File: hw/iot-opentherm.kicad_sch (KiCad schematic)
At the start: 32 parts, among them J1 USB_B_Micro, J2 Conn_01x02, J3 Conn_01x03, J4 Conn_02x06_Odd_Even, J5 Conn_01x02, Q1 BC858, U1 AMS1117-3.3, U2 ESP-12S, U3 PC817, U4 PC817

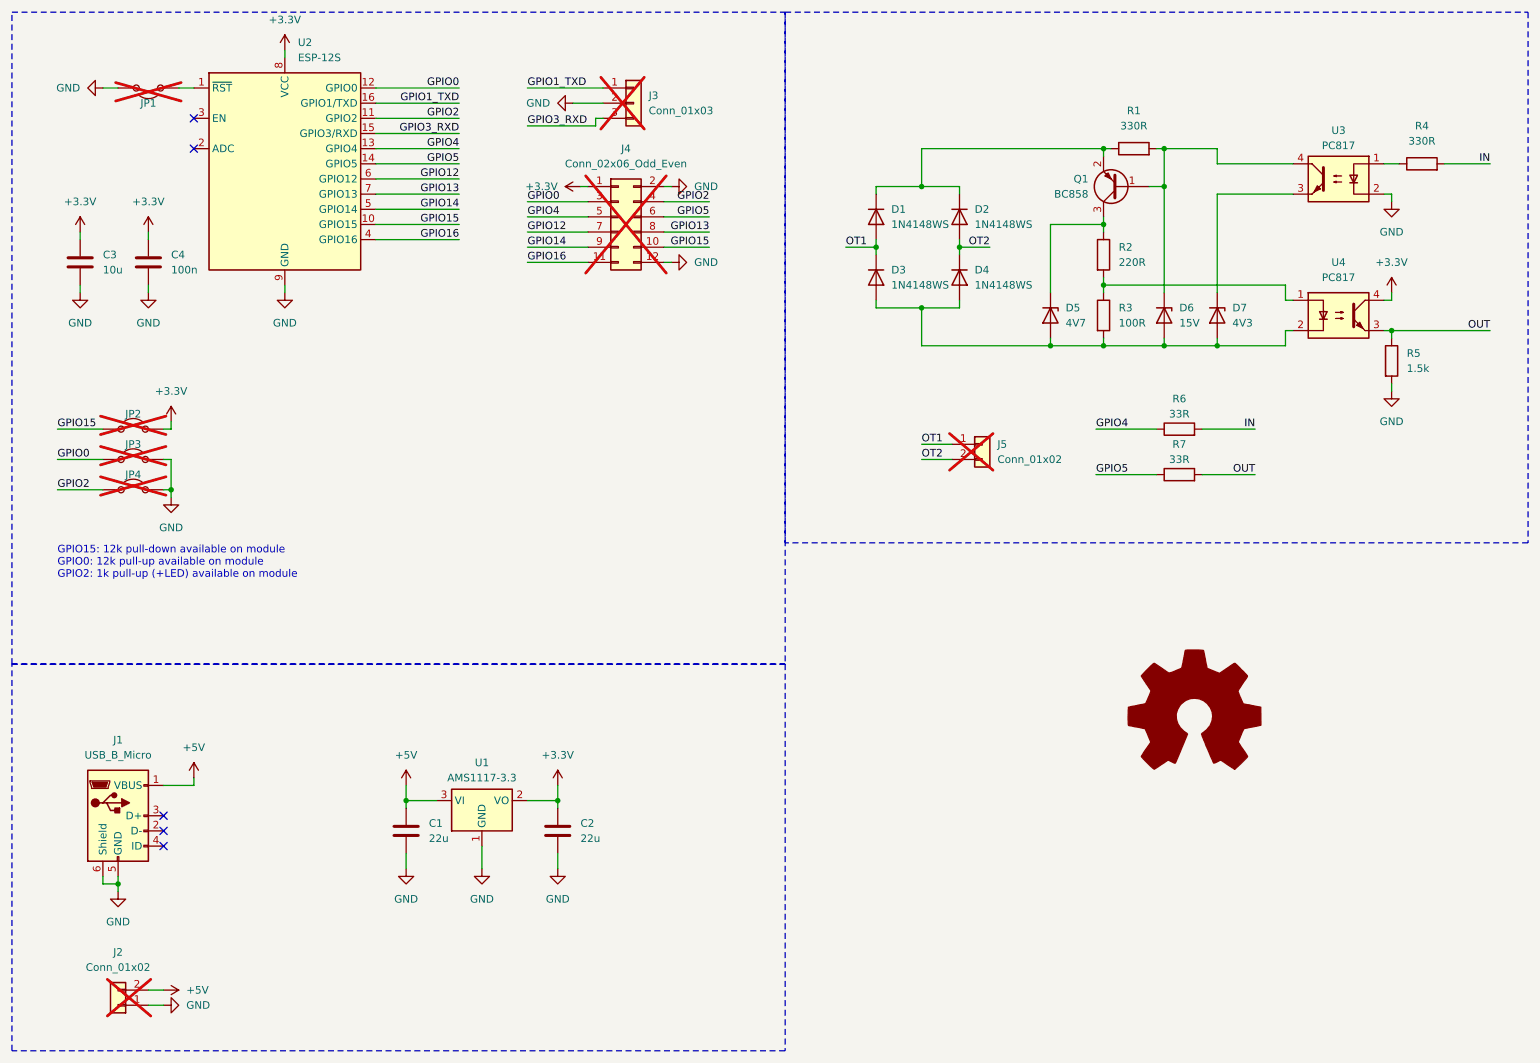
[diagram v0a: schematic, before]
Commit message: Fixes after running first version
1. Corrected footprint for D1, D2, D3, D4 to bigger one
2. Added connectors for OTx and +5VDC.
3. GPIOs for OT communication swapped to be aligned with Ihor's Melnyk
adapter design and Arthur Rump FW solution
4. Added labels for OTx and +5VDC
5. ERC: no regression
6. DRC: two more issues

Signed-off-by: Zbigniew Lukwinski <elezbyl@gmail.com>
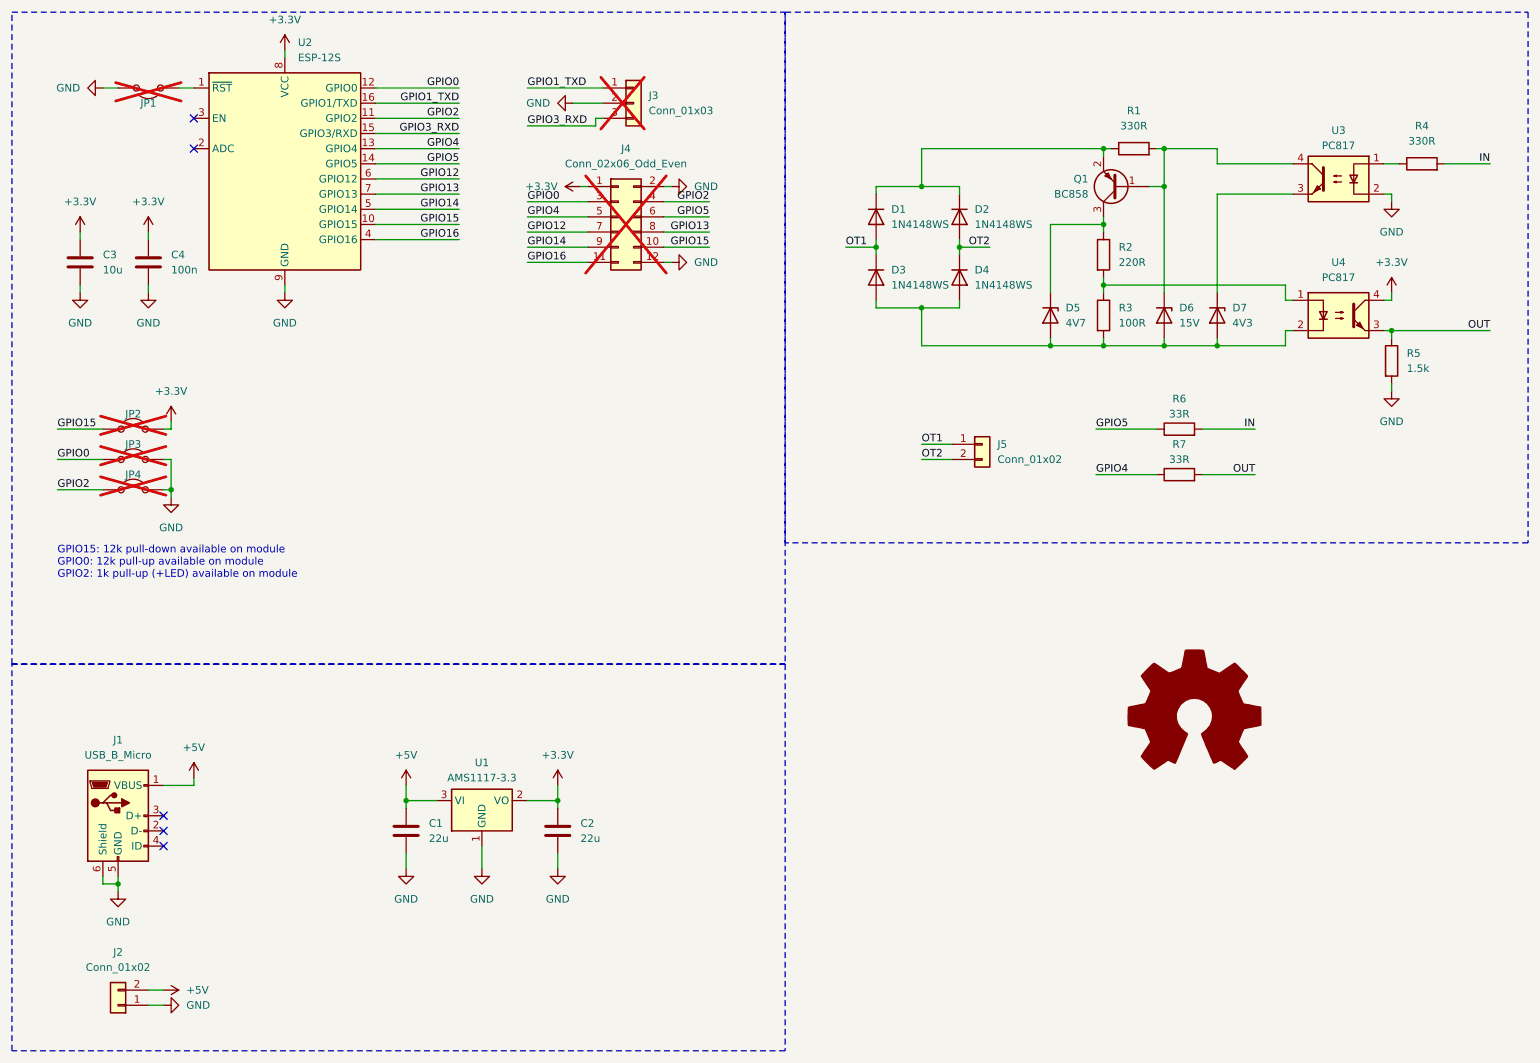
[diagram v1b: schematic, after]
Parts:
- D1, D2, D3, D4: footprint Diode_SMD:D_SOD-323 -> Diode_SMD:D_SOD-323_HandSoldering
- J2, J5: footprint Connector_PinHeader_2.54mm:PinHeader_1x02_P2.54mm_Vertical -> Connector_TE-Connectivity_:TE_282834-2; Farnell (none) -> 2112482; LCSC (none) -> C592983; Mouser (none) -> 571-282834-2; now fitted
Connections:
- net GPIO4: now also R7.1; no longer R6.1
- net GPIO5: now also R6.1; no longer R7.1
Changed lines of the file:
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@@
 		(title "IoT OpenTherm")
 		(date "2024-10-07")
-		(rev "1.00")
+		(rev "1.01")
 		(company "Elezbyl")
 	)
@@
 		)
 	)
-	(label "GPIO5"
+	(label "GPIO4"
 		(at 205.74 95.25 0)
 		(fields_autoplaced yes)
@@
 		)
 	)
-	(label "GPIO4"
+	(label "GPIO5"
 		(at 205.74 87.63 0)
 		(fields_autoplaced yes)
@@
 		(at 222.25 135.89 0)
 		(unit 1)
-		(exclude_from_sim no)
+		(exclude_from_sim yes)
 		(in_bom no)
 		(on_board no)
@@
 			)
 		)
-		(property "Sim.Enable" "0"
-			(at 222.25 135.89 0)
-			(effects
-				(font
-					(size 1.27 1.27)
-				)
-				(hide yes)
-			)
-		)
 		(instances
 			(project ""
@@
 		(in_bom yes)
 		(on_board yes)
-		(dnp yes)
+		(dnp no)
 		(fields_autoplaced yes)
 		(property "Reference" "J5"
@@
 			)
 		)
-		(property "Footprint" "Connector_PinHeader_2.54mm:PinHeader_1x02_P2.54mm_Vertical"
+		(property "Footprint" "Connector_TE-Connectivity_:TE_282834-2"
 			(at 186.69 90.17 0)
 			(effects
@@
 			)
 		)
+		(property "LCSC" "C592983"
+			(at 186.69 90.17 0)
+			(effects
+				(font
+					(size 1.27 1.27)
+				)
+				(hide yes)
+			)
+		)
+		(property "Farnell" "2112482"
+			(at 186.69 90.17 0)
+			(effects
+				(font
+					(size 1.27 1.27)
+				)
+				(hide yes)
+			)
+		)
+		(property "Mouser" "571-282834-2"
+			(at 186.69 90.17 0)
+			(effects
+				(font
+					(size 1.27 1.27)
+				)
+				(hide yes)
+			)
+		)
 		(pin "1"
 		)
@@
 			)
 		)
-		(property "Footprint" "Diode_SMD:D_SOD-323"
+		(property "Footprint" "Diode_SMD:D_SOD-323_HandSoldering"
 			(at 178.435 62.23 0)
 			(effects
@@
 			)
 		)
-		(property "Footprint" "Diode_SMD:D_SOD-323"
+		(property "Footprint" "Diode_SMD:D_SOD-323_HandSoldering"
 			(at 164.465 62.23 0)
 			(effects
@@
 		(in_bom yes)
 		(on_board yes)
-		(dnp yes)
+		(dnp no)
 		(fields_autoplaced yes)
 		(property "Reference" "J2"
@@
 			)
 		)
-		(property "Footprint" "Connector_PinHeader_2.54mm:PinHeader_1x02_P2.54mm_Vertical"
+		(property "Footprint" "Connector_TE-Connectivity_:TE_282834-2"
 			(at 41.91 184.15 0)
 			(effects
@@
 			)
 		)
+		(property "LCSC" "C592983"
+			(at 41.91 184.15 0)
+			(effects
+				(font
+					(size 1.27 1.27)
+				)
+				(hide yes)
+			)
+		)
+		(property "Farnell" "2112482"
+			(at 41.91 184.15 0)
+			(effects
+				(font
+					(size 1.27 1.27)
+				)
+				(hide yes)
+			)
+		)
+		(property "Mouser" "571-282834-2"
+			(at 41.91 184.15 0)
+			(effects
+				(font
+					(size 1.27 1.27)
+				)
+				(hide yes)
+			)
+		)
 		(pin "1"
 		)
@@
 			)
 		)
-		(property "Footprint" "Diode_SMD:D_SOD-323"
+		(property "Footprint" "Diode_SMD:D_SOD-323_HandSoldering"
 			(at 178.435 52.07 0)
 			(effects
@@
 			)
 		)
-		(property "Footprint" "Diode_SMD:D_SOD-323"
+		(property "Footprint" "Diode_SMD:D_SOD-323_HandSoldering"
 			(at 164.465 52.07 0)
 			(effects
